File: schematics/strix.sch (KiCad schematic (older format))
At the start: 23 parts

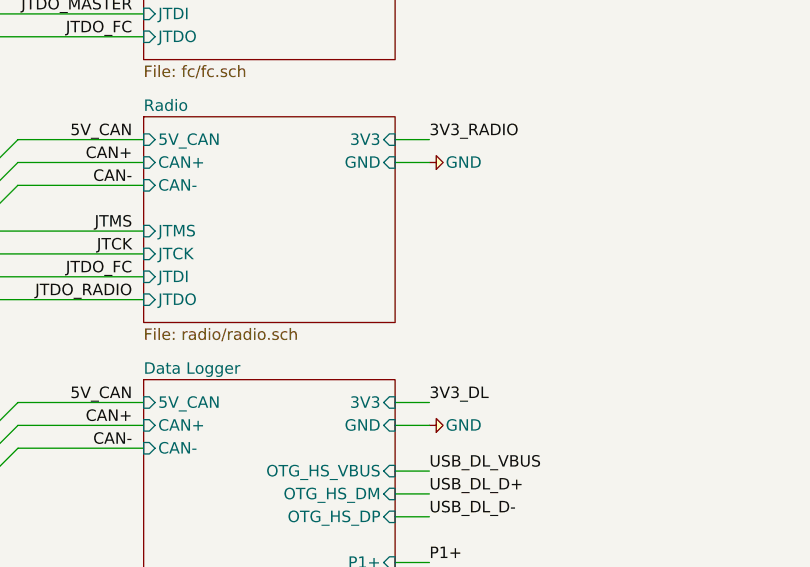
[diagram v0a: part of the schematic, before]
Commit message: Remove telemetry power amp
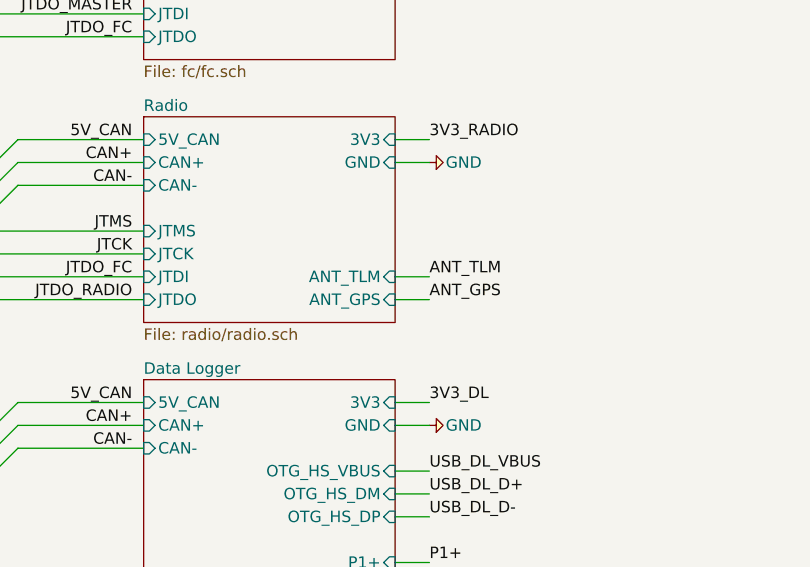
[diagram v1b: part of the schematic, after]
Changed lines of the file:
@@
 	1    0    0    -1
 $EndComp
-Wire Bus Line
-	1200 700  1200 7500
-Wire Bus Line
-	1000 1400 1000 7100
 $Sheet
 S 1850 800  1100 900
@@
 F9 "GND" I R 2950 2150 50
 F10 "JTDO" I L 1850 2750 50
+F11 "ANT_TLM" I R 2950 2650 50
+F12 "ANT_GPS" I R 2950 2750 50
 $EndSheet
 $Sheet
@@
 F10 "JTDR" I L 1850 7200 50
 $EndSheet
+Wire Wire Line
+	2950 2650 3100 2650
+Wire Wire Line
+	3100 2750 2950 2750
+Text Label 3100 2650 0    50   ~ 0
+ANT_TLM
+Text Label 3100 2750 0    50   ~ 0
+ANT_GPS
+Wire Bus Line
+	1200 700  1200 7500
+Wire Bus Line
+	1000 1400 1000 7100
 $EndSCHEMATC

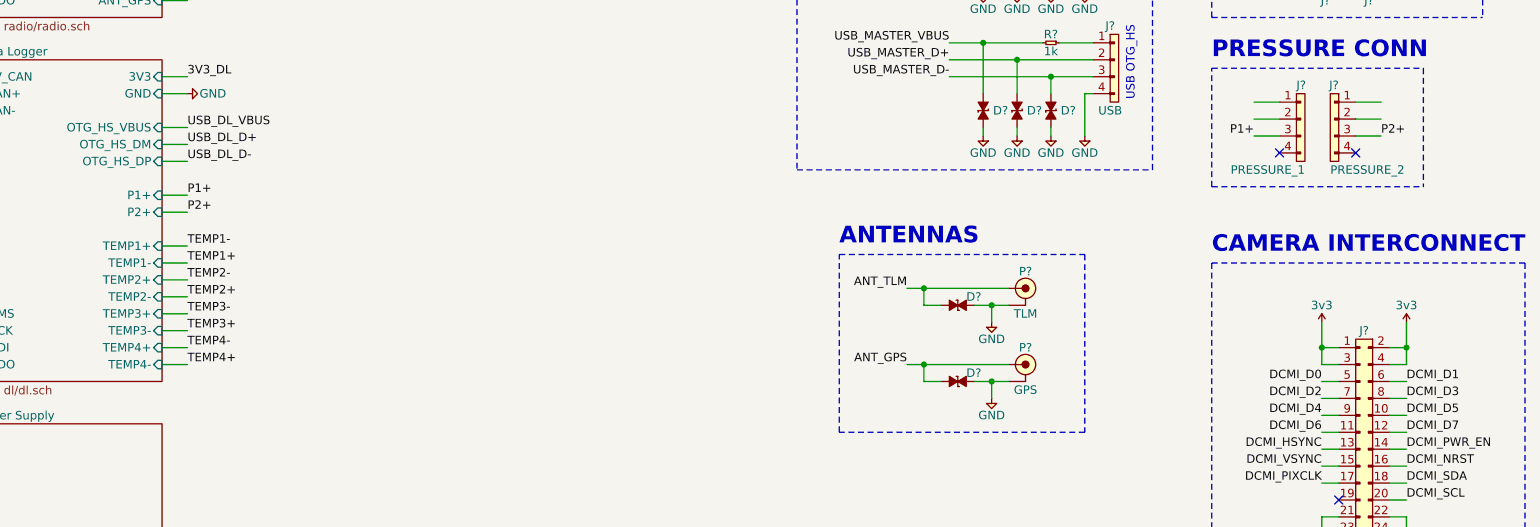
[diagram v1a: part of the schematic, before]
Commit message: Add sensor front-ends
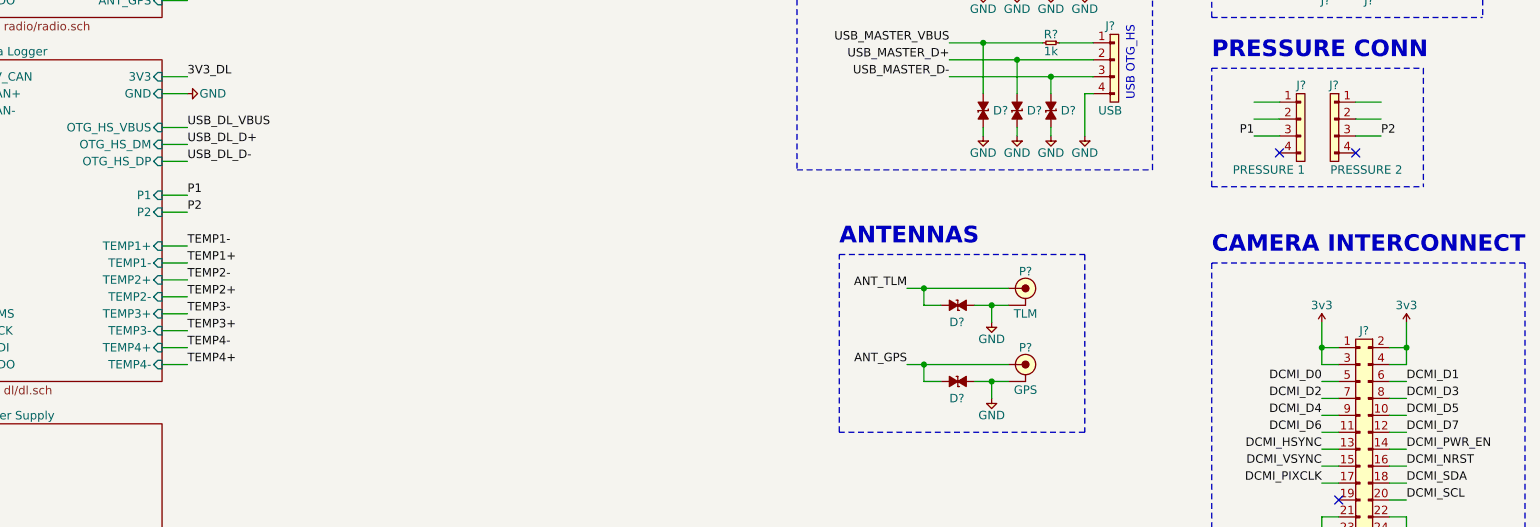
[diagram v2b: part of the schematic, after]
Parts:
- J?: value PRESSURE_1 -> PRESSURE 1
- J?: value PRESSURE_2 -> PRESSURE 2
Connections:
- net P1+ renamed P1
- net P2+ renamed P2
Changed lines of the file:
@@
 	3100 3700 2950 3700
 Text Label 3100 4000 0    50   ~ 0
-P2+
+P2
 Text Label 3100 3900 0    50   ~ 0
-P1+
+P1
 Wire Wire Line
 	2950 4000 3100 4000
@@
 Text Label 1800 1600 2    50   ~ 0
 JTDO_FC
-$Comp
-L cusf-kicad:CONN_01x04 J?
-U 1 1 60D6FAD8
-P 9650 3350
-F 0 "J?" H 9650 3450 50  0000 R CNN
-F 1 "PRESSURE_1" H 9600 2950 50  0000 L CNN
-F 2 "" H 9650 3350 50  0001 C CNN
-F 3 "~" H 9650 3350 50  0001 C CNN
-	1    9650 3350
-	-1   0    0    -1
-$EndComp
 Text Label 9400 3550 2    50   ~ 0
-P1+
+P1
 Wire Wire Line
 	9550 3450 9400 3450
@@
 P 9900 3350
 F 0 "J?" H 9900 3450 50  0000 R CNN
-F 1 "PRESSURE_2" H 9850 2950 50  0000 L CNN
+F 1 "PRESSURE 2" H 9850 2950 50  0000 L CNN
 F 2 "" H 9900 3350 50  0001 C CNN
 F 3 "~" H 9900 3350 50  0001 C CNN
@@
 $EndComp
 Text Label 10150 3550 0    50   ~ 0
-P2+
+P2
 Wire Wire Line
 	10000 3450 10150 3450
@@
 AR Path="/6013B1C8/60307A57" Ref="D?"  Part="1"
 AR Path="/60307A57" Ref="D?"  Part="1"
-F 0 "D?" H 7700 4600 50  0000 L CNN
+F 0 "D?" H 7600 4450 50  0000 L CNN
 F 1 "ESD_DIODE" H 7600 4450 50  0001 L CNN
 F 2 "agg:0402" H 7600 4350 50  0001 L CNN
@@
 AR Path="/6013B1C8/60384153" Ref="D?"  Part="1"
 AR Path="/60384153" Ref="D?"  Part="1"
-F 0 "D?" H 7700 5050 50  0000 L CNN
+F 0 "D?" H 7600 4900 50  0000 L CNN
 F 1 "ESD_DIODE" H 7600 4900 50  0001 L CNN
 F 2 "agg:0402" H 7600 4800 50  0001 L CNN
@@
 F19 "OTG_HS_DM" I R 2950 3600 50
 F20 "OTG_HS_DP" I R 2950 3700 50
-F21 "P1+" I R 2950 3900 50
-F22 "P2+" I R 2950 4000 50
-F23 "JTDO" I L 1850 4900 50
+F21 "JTDO" I L 1850 4900 50
+F22 "P1" I R 2950 3900 50
+F23 "P2" I R 2950 4000 50
 $EndSheet
 $Sheet
@@
 Wire Bus Line
 	1000 1400 1000 7100
+$Comp
+L cusf-kicad:CONN_01x04 J?
+U 1 1 60D6FAD8
+P 9650 3350
+F 0 "J?" H 9650 3450 50  0000 R CNN
+F 1 "PRESSURE 1" H 9600 2950 50  0000 L CNN
+F 2 "" H 9650 3350 50  0001 C CNN
+F 3 "~" H 9650 3350 50  0001 C CNN
+	1    9650 3350
+	-1   0    0    -1
+$EndComp
 $EndSCHEMATC

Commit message: Fix pressure connectors
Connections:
- net P1+: now reaches J?.1
- net P1-: now reaches J?.2
- net P2+: now reaches J?.1
- net P2-: now reaches J?.2
- net P1: no longer names the net of J?.3
- net P2: no longer names the net of J?.3
- no-connect marks 3 -> 5
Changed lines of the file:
@@
 Wire Wire Line
 	3100 3700 2950 3700
+Text Label 3100 4100 0    50   ~ 0
+P2-
 Text Label 3100 4000 0    50   ~ 0
-P2
-Text Label 3100 3900 0    50   ~ 0
-P1
+P2+
 Wire Wire Line
-	2950 4000 3100 4000
+	2950 4100 3100 4100
 Wire Wire Line
-	2950 3900 3100 3900
+	2950 4000 3100 4000
 Text Label 3100 3700 0    50   ~ 0
 USB_DL_D-
@@
 Text Label 1800 1600 2    50   ~ 0
 JTDO_FC
-Text Label 9400 3550 2    50   ~ 0
-P1
+Text Label 9400 3350 2    50   ~ 0
+P1+
 Wire Wire Line
 	9550 3450 9400 3450
-Wire Wire Line
-	9550 3550 9400 3550
 $Comp
 L cusf-kicad:CONN_01x02 J?
@@
 	1    0    0    -1
 $EndComp
-Text Label 10150 3550 0    50   ~ 0
-P2
-Wire Wire Line
-	10000 3450 10150 3450
-Wire Wire Line
-	10000 3550 10150 3550
 Wire Wire Line
 	9550 3350 9400 3350
-Wire Wire Line
-	10000 3350 10150 3350
 NoConn ~ 10000 3650
 NoConn ~ 9550 3650
@@
 F20 "OTG_HS_DP" I R 2950 3700 50
 F21 "JTDO" I L 1850 4900 50
-F22 "P1" I R 2950 3900 50
-F23 "P2" I R 2950 4000 50
+F22 "P1+" I R 2950 3800 50
+F23 "P1-" I R 2950 3900 50
+F24 "P2+" I R 2950 4000 50
+F25 "P2-" I R 2950 4100 50
 $EndSheet
 $Sheet
@@
 Text Label 3100 2750 0    50   ~ 0
 ANT_GPS
-Wire Bus Line
-	1200 700  1200 7500
-Wire Bus Line
-	1000 1400 1000 7100
 $Comp
 L cusf-kicad:CONN_01x04 J?
@@
 	-1   0    0    -1
 $EndComp
+Text Label 9400 3450 2    50   ~ 0
+P1-
+NoConn ~ 9550 3550
+Text Label 10150 3350 0    50   ~ 0
+P2+
+Wire Wire Line
+	10000 3450 10150 3450
+Wire Wire Line
+	10000 3350 10150 3350
+Text Label 10150 3450 0    50   ~ 0
+P2-
+NoConn ~ 10000 3550
+Text Label 3100 3800 0    50   ~ 0
+P1+
+Wire Wire Line
+	2950 3900 3100 3900
+Wire Wire Line
+	2950 3800 3100 3800
+Text Label 3100 3900 0    50   ~ 0
+P1-
+Wire Bus Line
+	1200 700  1200 7500
+Wire Bus Line
+	1000 1400 1000 7100
 $EndSCHEMATC
